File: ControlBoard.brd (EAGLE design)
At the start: 115.2 x 113 mm, 98 parts, among them CON1 CONN_20, CON2 CONN_20, CON3 CONN_20, CON4 CONN_20, CON5 CONN_2

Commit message: Removed lots of routes
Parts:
- moved U$34 4.19 mm to (47.8, 104.9), turned to 180 degrees
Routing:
- net N$16: track 64.0 -> 0.00 mm
- net N$15: track 58.7 -> 0.00 mm
- net LED_CTRL_7: track 56.4 -> 0.00 mm
- net N$9: track 55.9 -> 0.00 mm
- net N$10: track 55.8 -> 0.00 mm
- net N$14: track 54.6 -> 0.00 mm
- net N$13: track 52.1 -> 0.00 mm
- net N$11: track 51.2 -> 0.00 mm
- net N$12: track 50.7 -> 0.00 mm
- net LED_CTRL_6: track 41.6 -> 0.00 mm, vias 1 -> 0
- net LED_CTRL_8: track 40.3 -> 0.00 mm, vias 2 -> 0
- net LED_CTRL_4: track 35.3 -> 0.00 mm, vias 1 -> 0
- net LED_CTRL_5: track 33.9 -> 0.00 mm, vias 1 -> 0
- net LED_CTRL_17: track 40.0 -> 8.16 mm, vias 2 -> 0
- net LED_CTRL_18: track 34.5 -> 5.41 mm, vias 1 -> 0
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
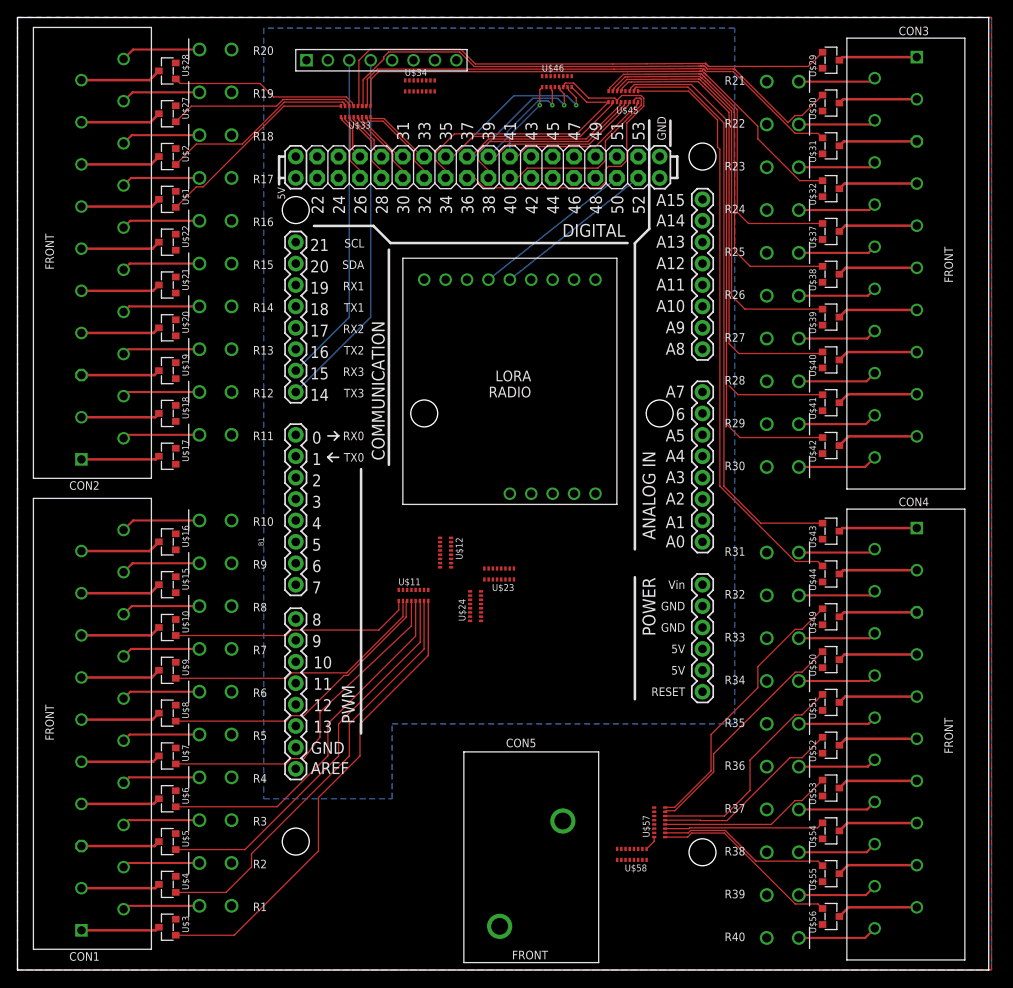
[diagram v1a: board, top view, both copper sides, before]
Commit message: Final refinements before first order
— Connected DFU and MOD pins of BLE UART board
— Tented vias
— Fixed DRC stop mask errors
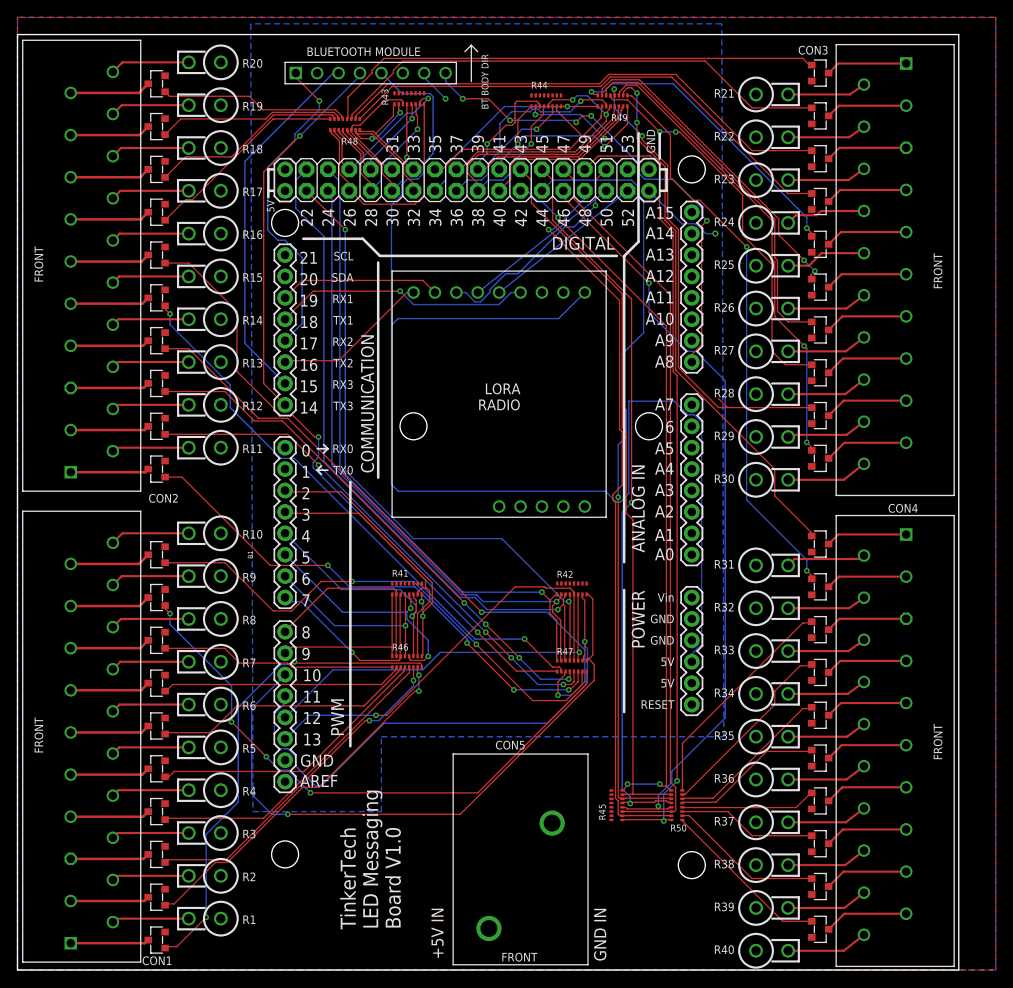
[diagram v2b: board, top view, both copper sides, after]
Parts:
- removed U$11, U$23, U$33, U$45, U$57: 10, TinkerTech:1506_X8
- removed U$12, U$24, U$34, U$46, U$58: 4.7k, TinkerTech:1506_X8
- added R41, R42, R43, R44, R45: 4.7k, TinkerTech:1506_X8
- added R46, R47, R48, R49, R50: 10, TinkerTech:1506_X8
- moved R6 1.98 mm to (22.9, 31.5)
- moved U$62 1.98 mm to (41.9, 106.4)
- moved U$64 1.98 mm to (57.1, 68.3)
- moved CON1 1.98 mm to (7.62, 27.7)
- moved CON2 1.98 mm to (7.62, 83.6)
- moved R10 1.98 mm to (22.9, 51.8)
- moved R11 1.98 mm to (22.9, 62.0)
- moved R12 1.98 mm to (22.9, 67.1)
- moved R13 1.98 mm to (22.9, 72.1)
- moved R14 1.98 mm to (22.9, 77.2)
- moved R16 1.98 mm to (22.9, 87.4)
- moved R17 1.98 mm to (22.9, 92.5)
- moved R18 1.98 mm to (22.9, 97.5)
- moved R19 1.98 mm to (22.9, 102.6)
- moved R20 1.98 mm to (22.9, 107.7)
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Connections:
- net RX1 renamed LORA_CS
- net TX1 renamed LORA_G0
- net TX2 renamed LORA_RST
- new net BTLE_DFU: B1.A8, U$62.DFU
- new net BTLE_MOD: B1.17, U$62.MOD
- net GND: now also R41.P$1, R41.P$2, R41.P$3, R41.P$4, R41.P$5, R41.P$6, R41.P$7, R41.P$8, R42.P$1, R42.P$2, R42.P$3, R42.P$4, R42.P$5, R42.P$6, R42.P$7, R42.P$8, R43.P$1, R43.P$2, R43.P$3, R43.P$4, R43.P$5, R43.P$6, R43.P$7, R43.P$8, R44.P$1, R44.P$2, R44.P$3, R44.P$4, R44.P$5, R44.P$6, R44.P$7, R44.P$8, R45.P$1, R45.P$2, R45.P$3, R45.P$4, R45.P$5, R45.P$6, R45.P$7, R45.P$8; no longer U$12.P$1, U$12.P$2, U$12.P$3, U$12.P$4, U$12.P$5, U$12.P$6, U$12.P$7, U$12.P$8, U$24.P$1, U$24.P$2, U$24.P$3, U$24.P$4, U$24.P$5, U$24.P$6, U$24.P$7, U$24.P$8, U$34.P$1, U$34.P$2, U$34.P$3, U$34.P$4, U$34.P$5, U$34.P$6, U$34.P$7, U$34.P$8, U$46.P$1, U$46.P$2, U$46.P$3, U$46.P$4, U$46.P$5, U$46.P$6, U$46.P$7, U$46.P$8, U$58.P$1, U$58.P$2, U$58.P$3, U$58.P$4, U$58.P$5, U$58.P$6, U$58.P$7, U$58.P$8
- net LED_CTRL_1: now also R41.P$16, R46.P$1; no longer U$11.P$1, U$12.P$16
- net LED_CTRL_10: now also R42.P$15, R47.P$2; no longer U$23.P$2, U$24.P$15
- net LED_CTRL_11: now also R42.P$14, R47.P$3; no longer U$23.P$3, U$24.P$14
- net LED_CTRL_12: now also R42.P$13, R47.P$4; no longer U$23.P$4, U$24.P$13
- net LED_CTRL_13: now also R42.P$12, R47.P$5; no longer U$23.P$5, U$24.P$12
- net LED_CTRL_14: now also R42.P$11, R47.P$6; no longer U$23.P$6, U$24.P$11
- net LED_CTRL_15: now also R42.P$10, R47.P$7; no longer U$23.P$7, U$24.P$10
- net LED_CTRL_16: now also R42.P$9, R47.P$8; no longer U$23.P$8, U$24.P$9
- net LED_CTRL_17: now also R43.P$16, R48.P$1; no longer U$33.P$1, U$34.P$16
- net LED_CTRL_18: now also R43.P$15, R48.P$2; no longer U$33.P$2, U$34.P$15
- net LED_CTRL_19: now also R43.P$14, R48.P$3; no longer U$33.P$3, U$34.P$14
- net LED_CTRL_2: now also R41.P$15, R46.P$2; no longer U$11.P$2, U$12.P$15
- net LED_CTRL_20: now also R43.P$13, R48.P$4; no longer U$33.P$4, U$34.P$13
- net LED_CTRL_21: now also R43.P$12, R48.P$5; no longer U$33.P$5, U$34.P$12
- net LED_CTRL_22: now also R43.P$11, R48.P$6; no longer U$33.P$6, U$34.P$11
- net LED_CTRL_23: now also R43.P$10, R48.P$7; no longer U$33.P$7, U$34.P$10
- net LED_CTRL_24: now also R43.P$9, R48.P$8; no longer U$33.P$8, U$34.P$9
- net LED_CTRL_25: now also R44.P$16, R49.P$1; no longer U$45.P$1, U$46.P$16
- net LED_CTRL_26: now also R44.P$15, R49.P$2; no longer U$45.P$2, U$46.P$15
- net LED_CTRL_27: now also R44.P$14, R49.P$3; no longer U$45.P$3, U$46.P$14
- net LED_CTRL_28: now also R44.P$13, R49.P$4; no longer U$45.P$4, U$46.P$13
- net LED_CTRL_29: now also R44.P$12, R49.P$5; no longer U$45.P$5, U$46.P$12
- net LED_CTRL_3: now also R41.P$14, R46.P$3; no longer U$11.P$3, U$12.P$14
- net LED_CTRL_30: now also R44.P$11, R49.P$6; no longer U$45.P$6, U$46.P$11
- net LED_CTRL_31: now also R44.P$10, R49.P$7; no longer U$45.P$7, U$46.P$10
- net LED_CTRL_32: now also R44.P$9, R49.P$8; no longer U$45.P$8, U$46.P$9
- net LED_CTRL_33: now also R45.P$16, R50.P$1; no longer U$57.P$1, U$58.P$16
- net LED_CTRL_34: now also R45.P$15, R50.P$2; no longer U$57.P$2, U$58.P$15
- net LED_CTRL_35: now also R45.P$14, R50.P$3; no longer U$57.P$3, U$58.P$14
- net LED_CTRL_36: now also R45.P$13, R50.P$4; no longer U$57.P$4, U$58.P$13
- net LED_CTRL_37: now also R45.P$12, R50.P$5; no longer U$57.P$5, U$58.P$12
- net LED_CTRL_38: now also R45.P$11, R50.P$6; no longer U$57.P$6, U$58.P$11
- net LED_CTRL_39: now also R45.P$10, R50.P$7; no longer U$57.P$7, U$58.P$10
- net LED_CTRL_4: now also R41.P$13, R46.P$4; no longer U$11.P$4, U$12.P$13
- net LED_CTRL_40: now also R45.P$9, R50.P$8; no longer U$57.P$8, U$58.P$9
- net LED_CTRL_5: now also R41.P$12, R46.P$5; no longer U$11.P$5, U$12.P$12
- net LED_CTRL_6: now also R41.P$11, R46.P$6; no longer U$11.P$6, U$12.P$11
- net LED_CTRL_7: now also R41.P$10, R46.P$7; no longer U$11.P$7, U$12.P$10
- net LED_CTRL_8: now also R41.P$9, R46.P$8; no longer U$11.P$8, U$12.P$9
- net LED_CTRL_9: now also R42.P$16, R47.P$1; no longer U$23.P$1, U$24.P$16
- net N$1: now also R46.P$16; no longer U$11.P$16
- net N$10: now also R47.P$15; no longer U$23.P$15
- net N$11: now also R47.P$14; no longer U$23.P$14
- net N$12: now also R47.P$13; no longer U$23.P$13
- net N$13: now also R47.P$12; no longer U$23.P$12
- net N$14: now also R47.P$11; no longer U$23.P$11
- net N$15: now also R47.P$10; no longer U$23.P$10
- net N$16: now also R47.P$9; no longer U$23.P$9
- net N$17: now also R48.P$16; no longer U$33.P$16
- net N$18: now also R48.P$15; no longer U$33.P$15
- net N$19: now also R48.P$14; no longer U$33.P$14
- net N$2: now also R46.P$15; no longer U$11.P$15
- net N$20: now also R48.P$13; no longer U$33.P$13
- net N$21: now also R48.P$12; no longer U$33.P$12
- net N$22: now also R48.P$11; no longer U$33.P$11
- net N$23: now also R48.P$10; no longer U$33.P$10
- net N$24: now also R48.P$9; no longer U$33.P$9
- net N$25: now also R49.P$16; no longer U$45.P$16
- net N$26: now also R49.P$15; no longer U$45.P$15
- net N$27: now also R49.P$14; no longer U$45.P$14
- net N$28: now also R49.P$13; no longer U$45.P$13
- net N$29: now also R49.P$12; no longer U$45.P$12
- net N$3: now also R46.P$14; no longer U$11.P$14
- net N$30: now also R49.P$11; no longer U$45.P$11
- net N$31: now also R49.P$10; no longer U$45.P$10
- net N$32: now also R49.P$9; no longer U$45.P$9
- net N$33: now also R50.P$16; no longer U$57.P$16
- net N$34: now also R50.P$15; no longer U$57.P$15
- net N$35: now also R50.P$14; no longer U$57.P$14
- net N$36: now also R50.P$13; no longer U$57.P$13
- net N$37: now also R50.P$12; no longer U$57.P$12
- net N$38: now also R50.P$11; no longer U$57.P$11
- net N$39: now also R50.P$10; no longer U$57.P$10
- net N$4: now also R46.P$13; no longer U$11.P$13
- net N$40: now also R50.P$9; no longer U$57.P$9
- net N$5: now also R46.P$12; no longer U$11.P$12
- net N$6: now also R46.P$11; no longer U$11.P$11
- net N$7: now also R46.P$10; no longer U$11.P$10
- net N$8: now also R46.P$9; no longer U$11.P$9
- net N$9: now also R47.P$16; no longer U$23.P$16
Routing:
- net MCU_5V: track 0.00 -> 159.6 mm
- net LED_CTRL_40: track 1.78 -> 95.3 mm, vias 0 -> 2
- net LED_CTRL_35: track 0.00 -> 93.1 mm, vias 0 -> 1
- net LED_CTRL_37: track 0.00 -> 91.1 mm, vias 0 -> 2
- net LED_CTRL_38: track 0.00 -> 88.0 mm
- net LED_CTRL_39: track 0.00 -> 86.8 mm, vias 0 -> 1
- net LED_CTRL_36: track 0.00 -> 86.7 mm, vias 0 -> 2
- net LED_CTRL_34: track 0.00 -> 85.5 mm
- net LED_CTRL_33: track 0.00 -> 85.1 mm, vias 0 -> 3
- net LED_CTRL_14: track 0.00 -> 80.6 mm, vias 0 -> 1
- net LED_CTRL_16: track 0.00 -> 76.3 mm, vias 0 -> 1
- net LED_CTRL_13: track 0.00 -> 76.1 mm, vias 0 -> 2
- net LED_CTRL_9: track 0.00 -> 75.5 mm, vias 0 -> 1
- net N$14: track 0.00 -> 75.4 mm, vias 0 -> 2
- net LED_CTRL_15: track 0.00 -> 74.9 mm, vias 0 -> 1
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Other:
- board size 115.2 x 113 mm -> 111.7 x 111 mm
- board text added: "+5V IN"
- board text added: "BLUETOOTH MODULE"
- board text added: "BT BODY DIR"
- board text added: "GND IN"
- board text added: "TinkerTech LED Messaging Board V1.0"
